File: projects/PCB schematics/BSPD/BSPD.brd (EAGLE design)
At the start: 99.1 x 99.1 mm, 83 parts, among them X1 5566-2, X2 5566-2, X3 5566-4

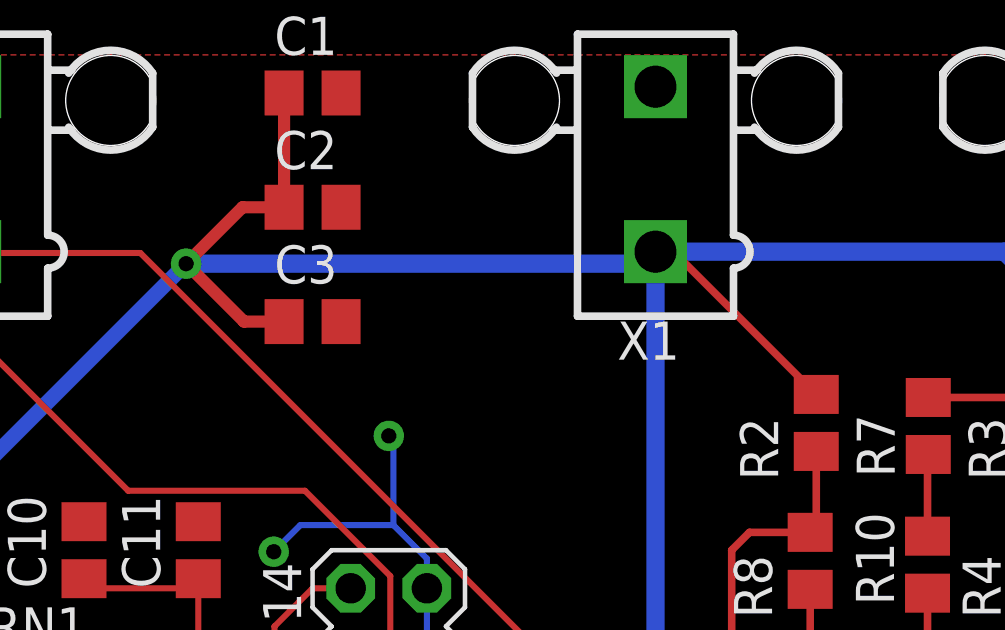
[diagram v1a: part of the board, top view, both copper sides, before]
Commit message: BSPD - Missing capacitor values added.
Component values were missing from sheet. Bypass capacitors, and LPF capacitors have been added.

--- SQUASH ---

PROJ - Added test files.

--- SQUASH ---

PROJ - Added test files.
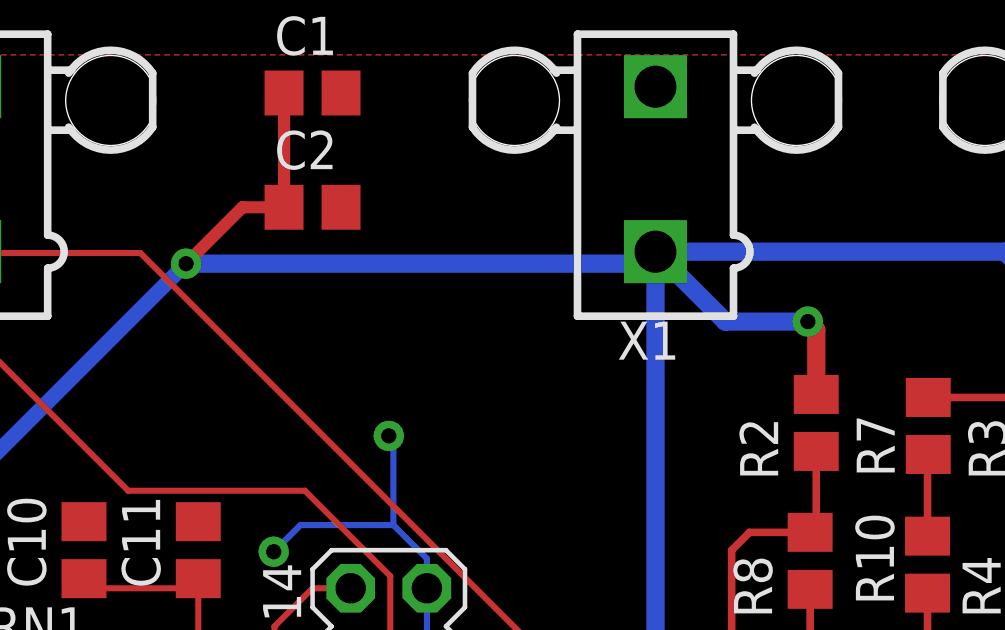
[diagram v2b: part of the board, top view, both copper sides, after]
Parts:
- removed C3: (no value), rcl:C0805
- C1, C4, C5, C6, C7: value (none) -> 1u
- C2: value (none) -> 0.1u
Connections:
- net +5V: no longer C3.1
- net GND: no longer C3.2
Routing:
- net +5V: track 483.8 -> 480.9 mm, vias 19 -> 20
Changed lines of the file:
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@@
 <attribute name="SPICEPREFIX" value="C" x="97.79" y="-25.4" size="1.778" layer="27" display="off"/>
 </element>
-<element name="C2" library="rcl" library_urn="urn:adsk.eagle:library:334" package="C0805" package3d_urn="urn:adsk.eagle:package:23617/2" value="" x="26.67" y="83.82" smashed="yes">
+<element name="C2" library="rcl" library_urn="urn:adsk.eagle:library:334" package="C0805" package3d_urn="urn:adsk.eagle:package:23617/2" value="0.1u" x="26.67" y="83.82" smashed="yes">
 <attribute name="NAME" x="25.4" y="85.09" size="1.27" layer="25"/>
 <attribute name="SPICEPREFIX" value="C" x="82.55" y="1.27" size="1.778" layer="27" display="off"/>
 <attribute name="VALUE" x="25.4" y="81.28" size="1.27" layer="27"/>
 </element>
-<element name="C3" library="rcl" library_urn="urn:adsk.eagle:library:334" package="C0805" package3d_urn="urn:adsk.eagle:package:23617/2" value="" x="26.67" y="80.01" smashed="yes">
-<attribute name="NAME" x="25.4" y="81.28" size="1.27" layer="25"/>
-<attribute name="SPICEPREFIX" value="C" x="87.63" y="-2.54" size="1.778" layer="27" display="off"/>
-<attribute name="VALUE" x="25.4" y="77.47" size="1.27" layer="27"/>
-</element>
-<element name="C4" library="rcl" library_urn="urn:adsk.eagle:library:334" package="C0805" package3d_urn="urn:adsk.eagle:package:23617/2" value="" x="57.15" y="40.64" smashed="yes">
+<element name="C4" library="rcl" library_urn="urn:adsk.eagle:library:334" package="C0805" package3d_urn="urn:adsk.eagle:package:23617/2" value="1u" x="57.15" y="40.64" smashed="yes">
 <attribute name="NAME" x="56.515" y="41.8846" size="1.27" layer="25"/>
 <attribute name="SPICEPREFIX" value="C" x="123.19" y="-41.91" size="1.778" layer="27" display="off"/>
 <attribute name="VALUE" x="55.88" y="38.1" size="1.27" layer="27"/>
 </element>
-<element name="C5" library="rcl" library_urn="urn:adsk.eagle:library:334" package="C0805" package3d_urn="urn:adsk.eagle:package:23617/2" value="" x="57.15" y="57.15" smashed="yes">
+<element name="C5" library="rcl" library_urn="urn:adsk.eagle:library:334" package="C0805" package3d_urn="urn:adsk.eagle:package:23617/2" value="1u" x="57.15" y="57.15" smashed="yes">
 <attribute name="NAME" x="55.88" y="58.42" size="1.27" layer="25"/>
 <attribute name="SPICEPREFIX" value="C" x="128.27" y="-25.4" size="1.778" layer="27" display="off"/>
 <attribute name="VALUE" x="55.88" y="54.61" size="1.27" layer="27"/>
 </element>
-<element name="C6" library="rcl" library_urn="urn:adsk.eagle:library:334" package="C0805" package3d_urn="urn:adsk.eagle:package:23617/2" value="" x="57.15" y="48.26" smashed="yes">
+<element name="C6" library="rcl" library_urn="urn:adsk.eagle:library:334" package="C0805" package3d_urn="urn:adsk.eagle:package:23617/2" value="1u" x="57.15" y="48.26" smashed="yes">
 <attribute name="NAME" x="55.88" y="49.53" size="1.27" layer="25"/>
 <attribute name="SPICEPREFIX" value="C" x="133.35" y="-34.29" size="1.778" layer="27" display="off"/>
 <attribute name="VALUE" x="55.88" y="45.72" size="1.27" layer="27"/>
 </element>
-<element name="C7" library="rcl" library_urn="urn:adsk.eagle:library:334" package="C0805" package3d_urn="urn:adsk.eagle:package:23617/2" value="" x="57.15" y="60.96" smashed="yes">
+<element name="C7" library="rcl" library_urn="urn:adsk.eagle:library:334" package="C0805" package3d_urn="urn:adsk.eagle:package:23617/2" value="1u" x="57.15" y="60.96" smashed="yes">
 <attribute name="NAME" x="55.88" y="62.23" size="1.27" layer="25"/>
 <attribute name="SPICEPREFIX" value="C" x="138.43" y="-21.59" size="1.778" layer="27" display="off"/>
@@
 <attribute name="OC_NEWARK" value="unknown" x="77.47" y="77.47" size="1.778" layer="27" display="off"/>
 </element>
-<element name="C1" library="rcl" library_urn="urn:adsk.eagle:library:334" package="C0805" package3d_urn="urn:adsk.eagle:package:23617/2" value="" x="26.67" y="87.63" smashed="yes">
+<element name="C1" library="rcl" library_urn="urn:adsk.eagle:library:334" package="C0805" package3d_urn="urn:adsk.eagle:package:23617/2" value="1u" x="26.67" y="87.63" smashed="yes">
 <attribute name="NAME" x="25.4" y="88.9" size="1.27" layer="25"/>
 <attribute name="SPICEPREFIX" value="C" x="26.67" y="87.63" size="1.778" layer="27" display="off"/>
@@
 <contactref element="X1" pad="2"/>
 <contactref element="R14" pad="1"/>
-<contactref element="C3" pad="2"/>
-<contactref element="C2" pad="2"/>
 <contactref element="C5" pad="2"/>
 <contactref element="C7" pad="2"/>
@@
 <contactref element="R32" pad="1"/>
 <contactref element="R34" pad="1"/>
-<contactref element="C1" pad="2"/>
 <polygon width="0.3048" layer="1" isolate="0.3048">
 <vertex x="5.08" y="88.9"/>
@@
 <wire x1="95.9866" y1="34.29" x2="95.9866" y2="45.3644" width="0.2032" layer="16"/>
 <wire x1="95.9866" y1="45.3644" x2="95.504" y2="45.847" width="0.2032" layer="16"/>
+<contactref element="C2" pad="2"/>
+<contactref element="C1" pad="2"/>
 </signal>
 <signal name="+1.0V">
@@
 <contactref element="R16" pad="2"/>
 <contactref element="C2" pad="1"/>
-<contactref element="C3" pad="1"/>
-<contactref element="R2" pad="2"/>
 <contactref element="RN2" pad="1"/>
 <contactref element="SV3" pad="14"/>
@@
 <contactref element="R33" pad="2"/>
 <contactref element="C1" pad="1"/>
-<wire x1="38.7012" y1="82.34" x2="43.4594" y2="77.5818" width="0.254" layer="1"/>
 <via x="22.4536" y="81.9404" extent="1-16" drill="0.508"/>
-<wire x1="22.4536" y1="81.9404" x2="24.384" y2="80.01" width="0.4064" layer="1"/>
-<wire x1="24.384" y1="80.01" x2="25.72" y2="80.01" width="0.4064" layer="1"/>
 <wire x1="22.4536" y1="81.9404" x2="24.3332" y2="83.82" width="0.4064" layer="1"/>
 <wire x1="24.3332" y1="83.82" x2="25.72" y2="83.82" width="0.4064" layer="1"/>
@@
 <wire x1="7.7216" y1="68.6816" x2="7.62" y2="68.58" width="0.2032" layer="16"/>
 <wire x1="7.7216" y1="68.6816" x2="7.62" y2="68.6816" width="0.2032" layer="16"/>
-<wire x1="38.2016" y1="82.296" x2="38.608" y2="82.296" width="0.2032" layer="1"/>
-<wire x1="38.608" y1="82.296" x2="38.7012" y2="82.34" width="0.2032" layer="1"/>
-<wire x1="38.2016" y1="82.296" x2="38.1" y2="82.34" width="0.2032" layer="1"/>
 <via x="35.2044" y="56.9214" extent="1-16" drill="0.508"/>
 <wire x1="32.4612" y1="59.69" x2="32.4612" y2="46.228" width="0.508" layer="16"/>
@@
 <wire x1="65.8368" y1="69.4944" x2="68.6562" y2="66.675" width="0.6096" layer="16"/>
 <wire x1="68.6562" y1="66.675" x2="68.6816" y2="66.675" width="0.6096" layer="16"/>
+<contactref element="R2" pad="2"/>
+<wire x1="38.1" y1="82.34" x2="40.43" y2="80.01" width="0.6096" layer="16"/>
+<wire x1="40.43" y1="80.01" x2="43.18" y2="80.01" width="0.6096" layer="16"/>
+<via x="43.18" y="80.01" extent="1-16" drill="0.508"/>
+<wire x1="43.18" y1="80.01" x2="43.4594" y2="79.7306" width="0.6096" layer="1"/>
+<wire x1="43.4594" y1="79.7306" x2="43.4594" y2="77.5818" width="0.6096" layer="1"/>
 </signal>
 <signal name="BSE_PROCESSED">

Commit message: BSPD - Changed OP amp to rail-to-rail.
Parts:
- OP1, OP2, OP3: value OP11D -> MCP6L04T-E/SLD; device linear:SO14 -> IowaFormula:SO14
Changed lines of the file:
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@@
 <?xml version="1.0" encoding="utf-8"?>
 <!DOCTYPE eagle SYSTEM "eagle.dtd">
-<eagle version="9.3.2">
+<eagle version="9.4.0">
 <drawing>
 <settings>
@@
 <attribute name="SPICEPREFIX" value="C" x="-10.16" y="77.47" size="1.778" layer="27" rot="R180" display="off"/>
 </element>
-<element name="OP2" library="linear" library_urn="urn:adsk.eagle:library:262" package="SO14" package3d_urn="urn:adsk.eagle:package:16406/2" value="OP11D" x="46.5582" y="40.64" smashed="yes" rot="R270">
+<element name="OP2" library="IowaFormula" package="SO14" package3d_urn="urn:adsk.eagle:package:16406/2" value="MCP6L04T-E/SLD" x="46.5582" y="40.64" smashed="yes" rot="R270">
 <attribute name="NAME" x="44.6532" y="45.212" size="1.27" layer="25"/>
 <attribute name="VALUE" x="47.1932" y="34.798" size="1.27" layer="27"/>
@@
 <attribute name="VALUE" x="75.692" y="26.416" size="1.27" layer="27" ratio="10" rot="R270"/>
 </element>
-<element name="OP1" library="linear" library_urn="urn:adsk.eagle:library:262" package="SO14" package3d_urn="urn:adsk.eagle:package:16406/2" value="OP11D" x="46.5582" y="54.61" smashed="yes" rot="R270">
+<element name="OP1" library="IowaFormula" package="SO14" package3d_urn="urn:adsk.eagle:package:16406/2" value="MCP6L04T-E/SLD" x="46.5582" y="54.61" smashed="yes" rot="R270">
 <attribute name="NAME" x="44.6532" y="59.182" size="1.27" layer="25"/>
 <attribute name="VALUE" x="44.6532" y="48.768" size="1.27" layer="27"/>
@@
 <attribute name="VALUE" x="84.455" y="53.594" size="1.27" layer="27" ratio="10" rot="R270"/>
 </element>
-<element name="OP3" library="linear" library_urn="urn:adsk.eagle:library:262" package="SO14" package3d_urn="urn:adsk.eagle:package:16406/2" value="OP11D" x="46.5582" y="29.21" smashed="yes" rot="R270">
+<element name="OP3" library="IowaFormula" package="SO14" package3d_urn="urn:adsk.eagle:package:16406/2" value="MCP6L04T-E/SLD" x="46.5582" y="29.21" smashed="yes" rot="R270">
 <attribute name="NAME" x="44.6532" y="33.782" size="1.27" layer="25"/>
 <attribute name="VALUE" x="44.6532" y="23.368" size="1.27" layer="27"/>

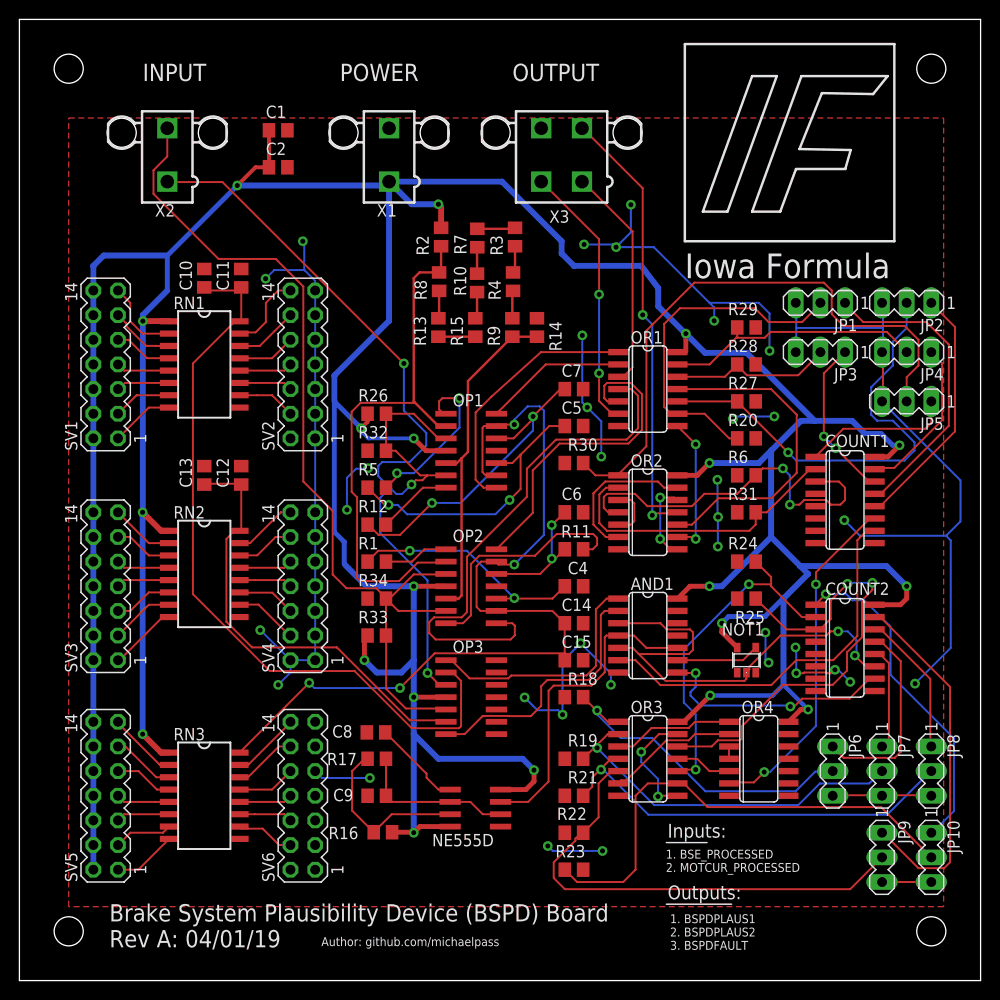
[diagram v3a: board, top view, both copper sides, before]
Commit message: PROJ - Silkscreen modifications - 50%.
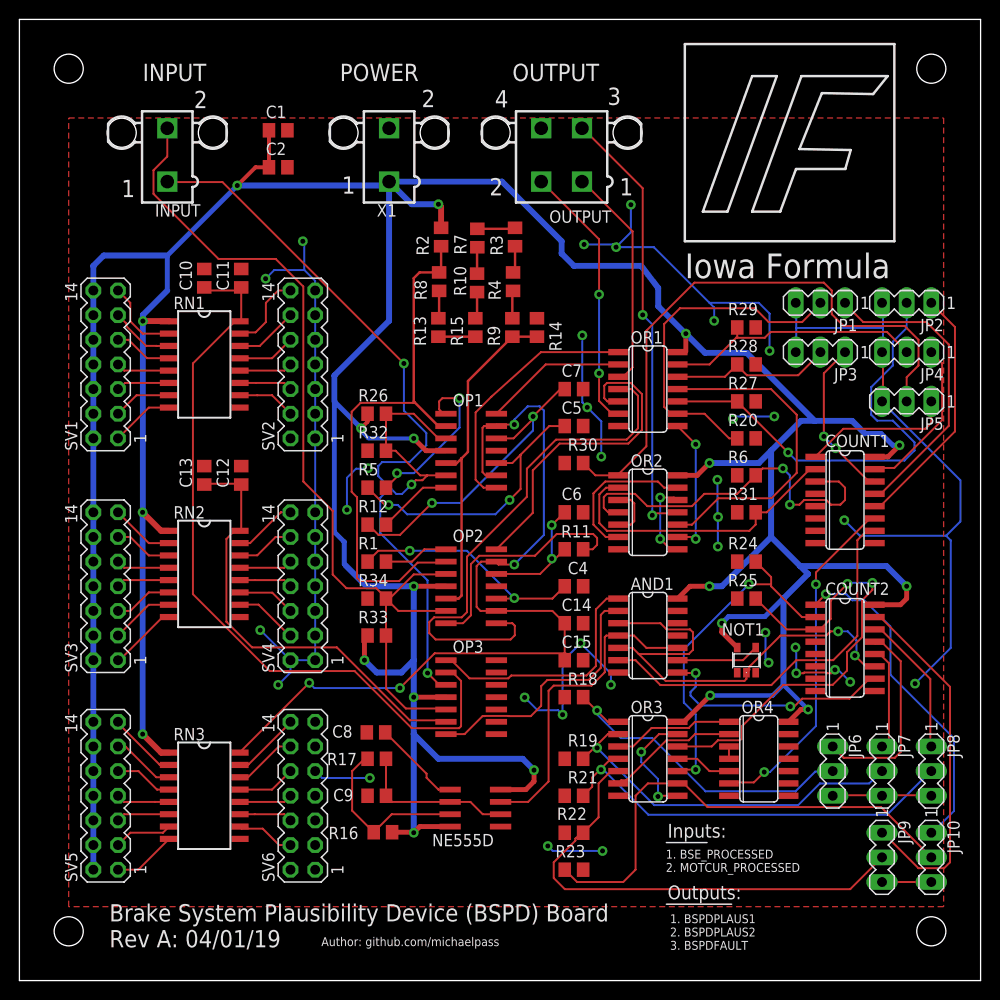
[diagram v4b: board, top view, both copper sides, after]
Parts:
- renumbered X2 to INPUT, X3 to OUTPUT
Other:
- board text added: "1"
- board text added: "2"
- board text added: "3"
- board text added: "4"
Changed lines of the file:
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@@
 <wire x1="78.4098" y1="79.248" x2="75.5142" y2="79.248" width="0.254" layer="25"/>
 <text x="68.58" y="72.39" size="2.54" layer="25" font="vector">Iowa Formula</text>
+<text x="10.5156" y="80.7466" size="1.778" layer="21">1</text>
+<text x="33.2232" y="81.1022" size="1.778" layer="21">1</text>
+<text x="61.849" y="80.9244" size="1.778" layer="21">1</text>
+<text x="48.4378" y="80.9244" size="1.778" layer="21">2</text>
+<text x="60.6044" y="90.2462" size="1.778" layer="21">3</text>
+<text x="48.9966" y="89.9922" size="1.778" layer="21">4</text>
+<text x="41.4528" y="90.0176" size="1.778" layer="21">2</text>
+<text x="17.9832" y="89.916" size="1.778" layer="21">2</text>
 </plain>
 <attributes>
@@
 </element>
 <element name="R25" library="rcl" library_urn="urn:adsk.eagle:library:334" package="R0805" package3d_urn="urn:adsk.eagle:package:23553/2" value="10k" x="74.93" y="39.37" smashed="yes">
-<attribute name="NAME" x="76.835" y="38.1" size="1.27" layer="25" rot="R180"/>
+<attribute name="NAME" x="73.025" y="40.64" size="1.27" layer="25"/>
 <attribute name="SPICEPREFIX" value="R" x="142.24" y="-25.4" size="1.778" layer="27" display="off"/>
 </element>
@@
 <attribute name="OC_NEWARK" value="unknown" x="74.93" y="77.47" size="1.778" layer="27" display="off"/>
 </element>
-<element name="X2" library="con-molex" library_urn="urn:adsk.eagle:library:165" package="5566-2" package3d_urn="urn:adsk.eagle:package:8078583/1" value="5566-2" x="15.24" y="85.09" smashed="yes">
+<element name="INPUT" library="con-molex" library_urn="urn:adsk.eagle:library:165" package="5566-2" package3d_urn="urn:adsk.eagle:package:8078583/1" value="5566-2" x="15.24" y="85.09" smashed="yes">
 <attribute name="MF" value="MOLEX" x="64.77" y="77.47" size="1.778" layer="27" display="off"/>
 <attribute name="MPN" value="" x="64.77" y="77.47" size="1.778" layer="27" display="off"/>
@@
 <attribute name="OC_NEWARK" value="unknown" x="64.77" y="77.47" size="1.778" layer="27" display="off"/>
 </element>
-<element name="X3" library="con-molex" library_urn="urn:adsk.eagle:library:165" package="5566-4" package3d_urn="urn:adsk.eagle:package:8078582/1" value="5566-4" x="55.88" y="85.09" smashed="yes">
+<element name="OUTPUT" library="con-molex" library_urn="urn:adsk.eagle:library:165" package="5566-4" package3d_urn="urn:adsk.eagle:package:8078582/1" value="5566-4" x="55.88" y="85.09" smashed="yes">
 <attribute name="MF" value="MOLEX" x="77.47" y="77.47" size="1.778" layer="27" display="off"/>
 <attribute name="MPN" value="" x="77.47" y="77.47" size="1.778" layer="27" display="off"/>
@@
 <contactref element="OP1" pad="6"/>
 <contactref element="R32" pad="2"/>
-<contactref element="X2" pad="1"/>
+<contactref element="INPUT" pad="1"/>
 <wire x1="37.78" y1="58.42" x2="37.78" y2="54.61" width="0.2032" layer="1"/>
 <wire x1="37.78" y1="58.42" x2="40.64" y2="58.42" width="0.2032" layer="1"/>
@@
 <contactref element="OP2" pad="6"/>
 <contactref element="R34" pad="2"/>
-<contactref element="X2" pad="2"/>
+<contactref element="INPUT" pad="2"/>
 <wire x1="37.78" y1="39.37" x2="39.05" y2="38.1" width="0.2032" layer="1"/>
 <wire x1="39.05" y1="38.1" x2="43.9582" y2="38.1" width="0.2032" layer="1"/>
@@
 <signal name="BSPDPLAUS1">
 <contactref element="OR1" pad="3"/>
-<contactref element="X3" pad="1"/>
+<contactref element="OUTPUT" pad="1"/>
 <wire x1="62.3824" y1="62.3824" x2="61.7728" y2="62.3824" width="0.2032" layer="1"/>
 <wire x1="63.1952" y1="63.1952" x2="62.3824" y2="62.3824" width="0.2032" layer="1"/>
@@
 <signal name="BSPDPLAUS2">
 <contactref element="OR1" pad="6"/>
-<contactref element="X3" pad="2"/>
+<contactref element="OUTPUT" pad="2"/>
 <wire x1="60.96" y1="58.5216" x2="61.5696" y2="58.5216" width="0.2032" layer="1"/>
 <wire x1="59.7408" y1="59.7408" x2="60.96" y2="58.5216" width="0.2032" layer="1"/>
@@
 <signal name="BSPDFAULT">
 <contactref element="OR2" pad="11"/>
-<contactref element="X3" pad="3"/>
+<contactref element="OUTPUT" pad="3"/>
 <wire x1="65.4304" y1="48.1584" x2="67.6656" y2="48.1584" width="0.2032" layer="1"/>
 <wire x1="65.2272" y1="47.9552" x2="65.4304" y2="48.1584" width="0.2032" layer="1"/>

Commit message: PROJ - Gerber files major milestone - 05/05/19.
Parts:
- AND1: value 74ALS09D -> 74ALS08D
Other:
- board text added: "Brake System Plausibility Device (BSPD) Board Rev A: 05/05/19"
- board text removed: "Brake System Plausibility Device (BSPD) Board Rev A: 04/01/19"
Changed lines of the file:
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@@
 <hole x="93.98" y="5.08" drill="3"/>
 <text x="9.271" y="3.429" size="1.778" layer="25" font="vector">Brake System Plausibility Device (BSPD) Board
-Rev A: 04/01/19</text>
+Rev A: 05/05/19</text>
 <text x="66.802" y="14.732" size="1.4224" layer="25" font="vector">Inputs:</text>
 <text x="66.802" y="8.382" size="1.4224" layer="25" font="vector">Outputs:</text>
@@
 <attribute name="VALUE" x="64.262" y="51.816" size="1.27" layer="27" ratio="10" rot="R270"/>
 </element>
-<element name="AND1" library="74xx-us" library_urn="urn:adsk.eagle:library:88" package="SO14" package3d_urn="urn:adsk.eagle:package:2917/1" value="74ALS09D" x="64.77" y="35.56" smashed="yes" rot="R270">
+<element name="AND1" library="74xx-us" library_urn="urn:adsk.eagle:library:88" package="SO14" package3d_urn="urn:adsk.eagle:package:2917/1" value="74ALS08D" x="64.77" y="35.56" smashed="yes" rot="R270">
 <attribute name="NAME" x="62.992" y="40.259" size="1.27" layer="25" ratio="10"/>
 <attribute name="VALUE" x="64.262" y="39.116" size="1.27" layer="27" ratio="10" rot="R270"/>
@@
 <wire x1="36.1188" y1="20.8788" x2="31.1912" y2="20.8788" width="0.2032" layer="16"/>
 <wire x1="31.1912" y1="20.8788" x2="30.48" y2="21.59" width="0.2032" layer="16"/>
-<wire x1="61.7728" y1="31.9024" x2="61.6966" y2="31.75" width="0.2032" layer="1"/>
-<wire x1="61.7728" y1="31.9024" x2="61.70931875" y2="31.7627" width="0.2032" layer="1"/>
 <via x="60.0964" y="13.3604" extent="1-16" drill="0.508"/>
 <via x="54.4576" y="13.8684" extent="1-16" drill="0.508"/>
